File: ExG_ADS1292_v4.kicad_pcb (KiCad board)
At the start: 2 copper layers, 31.8 x 19.6 mm, 64 parts, among them P1 CONN_2, P2 CONN_2, P3 CONN_2, P4 CONN_1, P5 CONN_01X04, U1 TPS63001, U2 ADS1291/2, U3 NRF528XX-QFAA, U4 MPU-9250, U5 TPS2294x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

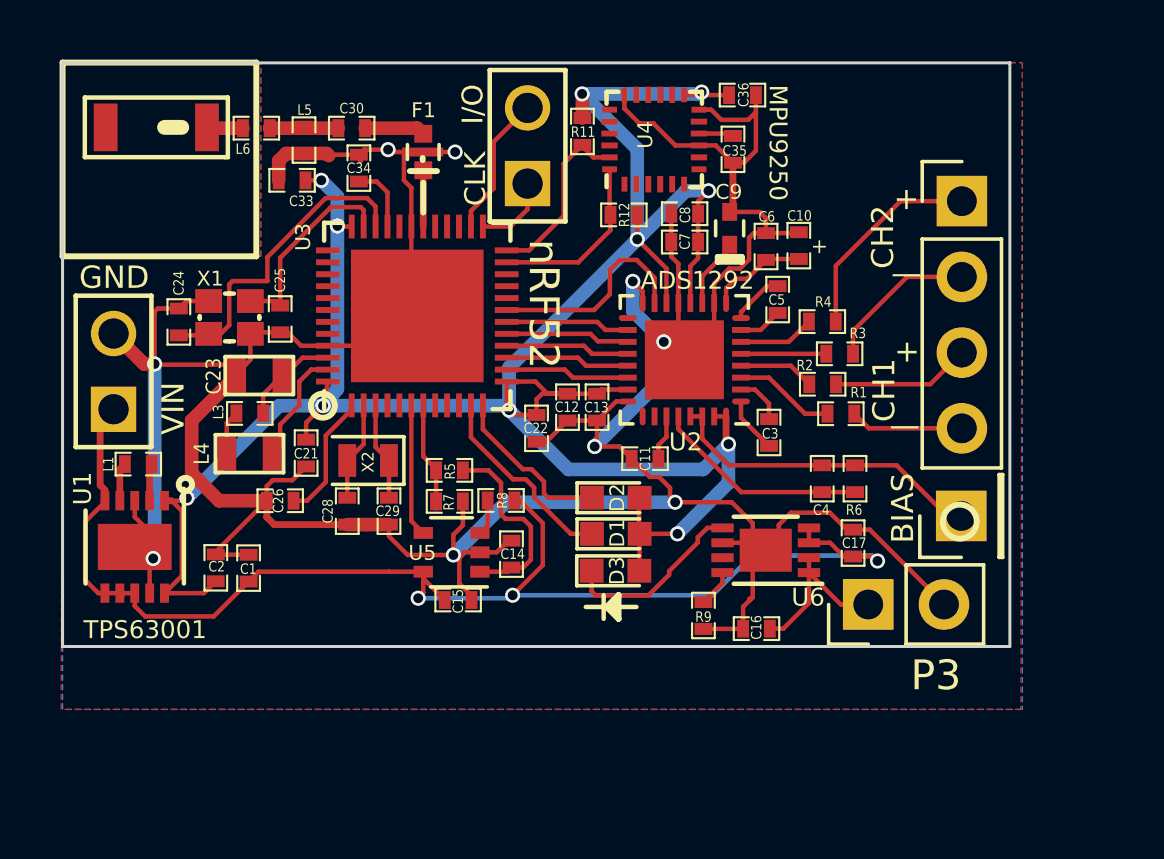
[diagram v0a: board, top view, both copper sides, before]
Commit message: Added updated recharging and load sharing circuit : extra components (Q1, D4, R10, C18).
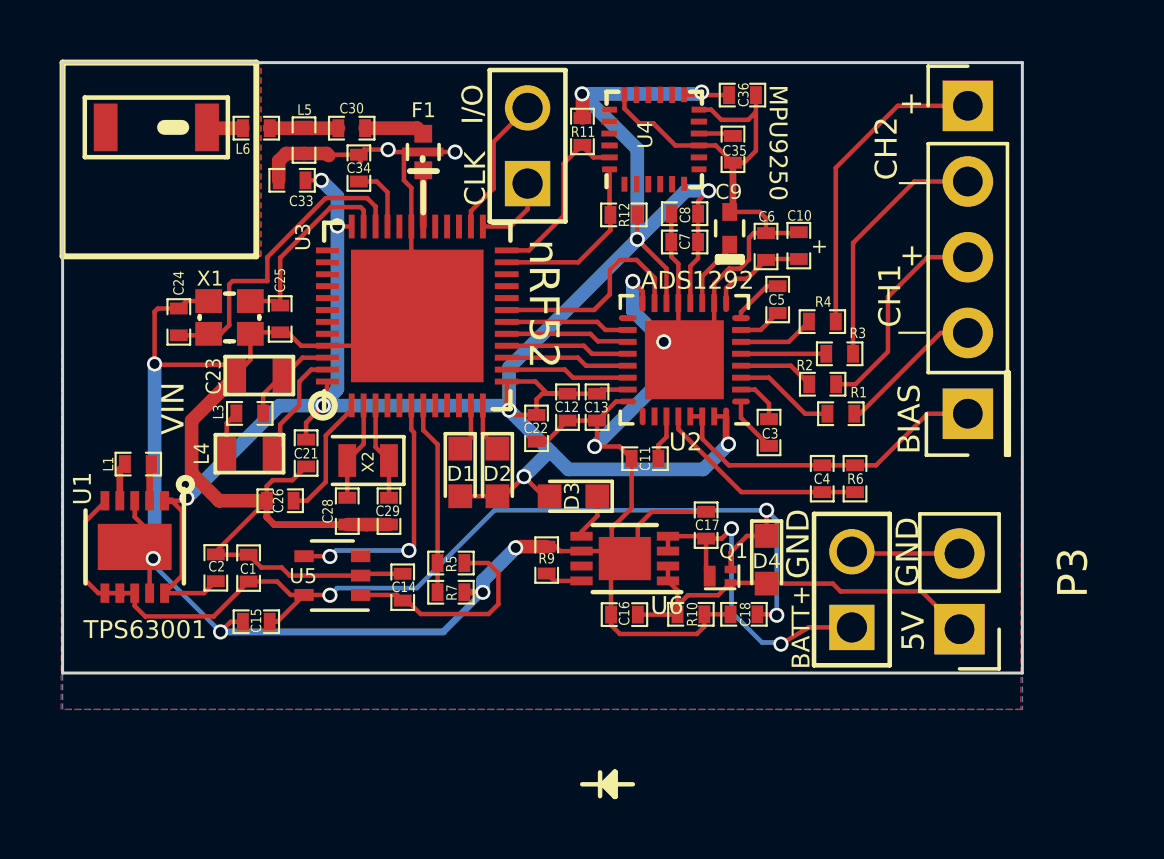
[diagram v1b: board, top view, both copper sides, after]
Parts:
- removed R8: N.C., SM0402
- added C18: 1.0uF, SM0402, F.Cu at (288.8, 144.0)
- added D4: D_Schottky, LEDs:LED_0603, F.Cu at (289.5, 142.2)
- added Q1: Q_PMOS_GDS, pwr_pads:X2-DFN1006, F.Cu at (288.0, 142.7)
- added R10: 100k, SM0402, F.Cu at (287.0, 144.0)
- moved P1 25.8 mm to (292.4, 143.2)
- moved C15 6.81 mm to (272.4, 144.3), turned to 180 degrees
- moved D1 5.61 mm to (279.2, 139.2), turned to 270 degrees
- moved R9 5.58 mm to (282.1, 142.2), turned to 90 degrees
- moved C17 4.97 mm to (287.5, 141.0)
- moved U6 4.74 mm to (284.8, 142.1)
- moved C16 4.45 mm to (284.8, 144.0)
- moved U5 4.08 mm to (274.9, 142.7)
- moved D2 4.06 mm to (280.5, 139.2), turned to 270 degrees
- moved C14 3.82 mm to (277.3, 143.1)
- moved P4 3.44 mm to (296.3, 137.3)
- moved P5 3.21 mm to (296.3, 127.0)
- moved P3 3.17 mm to (296.0, 144.5), turned to 180 degrees
- moved R5 3.11 mm to (278.9, 142.3)
- moved R7 3.05 mm to (278.9, 143.3)
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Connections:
- C17 pad 1: VCC -> /BATT_IN
- P1 pad 1: VCC -> /BATT_IN
- U6 pad 3: VCC -> /BATT_IN
- U6 pad 4: VCC -> /BATT_IN
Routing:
- net /BATT_IN: track 0.00 -> 11.5 mm, vias 0 -> 2
- net 5V_in_charge: track 5.62 -> 13.8 mm
- net VCC: track 44.5 -> 37.3 mm
- net /LED2: track 6.66 -> 1.60 mm
- net Net-(D3-Pad1): track 6.25 -> 1.56 mm
- net DGND: track 152.8 -> 157.3 mm, vias 9 -> 10
- net /LOAD_SW_CTRL: track 4.45 -> 8.58 mm, vias 0 -> 2
- net /LED3: track 5.63 -> 1.65 mm
- net /IN2: track 7.00 -> 10.5 mm
- net /IN2-: track 5.17 -> 8.42 mm
- net /AIN_BAT_DIV_VOLTAGE: track 3.77 -> 6.47 mm
- net DVDD: track 85.1 -> 82.4 mm
- net /IN1: track 4.66 -> 7.26 mm
- net Net-(R8-Pad1): track 1.20 -> 0.00 mm
- net /IN1-: track 3.81 -> 4.93 mm
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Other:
- board size 31.8 x 19.6 mm -> 32.2 x 20.5 mm
- board text added: "5V"
- board text added: "BATT+"

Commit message: Fixed load sharing circuit and PCB (final)
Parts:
- Q1: value Q_PMOS_GDS -> DMP21D5UFB4-7B
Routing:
- net DGND: track 157.3 -> 163.8 mm, vias 10 -> 11
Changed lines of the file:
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@@
     (links 185)
     (no_connects 0)
-    (area 265.849999 125.449999 297.730001 145.140001)
+    (area 264.8176 122.157123 320.907143 150.212501)
     (thickness 1.6)
     (drawings 47)
-    (tracks 546)
+    (tracks 552)
     (zones 0)
     (modules 67)
@@
   )
   (setup
-    (last_trace_width 0.152)
+    (last_trace_width 0.4572)
     (user_trace_width 0.152)
     (user_trace_width 0.229)
@@
       (effects (font (size 0.5 0.5) (thickness 0.08)))
     )
-    (fp_text value Q_PMOS_GDS (at 0.225 1.425 180) (layer F.Fab)
+    (fp_text value DMP21D5UFB4-7B (at 0.225 1.425 180) (layer F.Fab)
       (effects (font (size 1 1) (thickness 0.15)))
     )
@@
   (segment (start 280.9 131.8) (end 280.95 131.8) (width 0.152) (layer F.Cu) (net 54))
   (segment (start 280.9 131.8) (end 281.1 131.8) (width 0.1524) (layer F.Cu) (net 54))
+  (segment (start 287.49 140.57042) (end 287.49 140.08) (width 0.152) (layer F.Cu) (net 72))
+  (segment (start 290 139.53) (end 292.38 141.91) (width 0.229) (layer B.Cu) (net 72))
+  (segment (start 288.04 139.53) (end 290 139.53) (width 0.229) (layer B.Cu) (net 72))
+  (segment (start 287.74 139.83) (end 288.04 139.53) (width 0.229) (layer B.Cu) (net 72))
+  (via (at 287.74 139.83) (size 0.508) (drill 0.3302) (layers F.Cu B.Cu) (net 72))
+  (segment (start 287.49 140.08) (end 287.74 139.83) (width 0.152) (layer F.Cu) (net 72))
   (segment (start 284.30042 144.02) (end 284.30042 144.37042) (width 0.152) (layer F.Cu) (net 72))
   (segment (start 287.42958 144.42042) (end 287.42958 144.01) (width 0.152) (layer F.Cu) (net 72))

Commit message: Removed MPU9250 (EMG only with recharge circuit).
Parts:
- removed C35, C36: 100nF, SM0402
- removed R11, R12: 10k, SM0402
- removed U4: MPU-9250, Housings_DFN_QFN:QFN-24_3x3mm_Pitch0.4mm
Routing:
- net DVDD: track 82.4 -> 69.5 mm, vias 11 -> 9
- net DGND: track 163.8 -> 152.3 mm
- net /SCL: track 6.40 -> 0.25 mm
- net /SDI: track 5.98 -> 0.00 mm
- net Net-(C35-Pad1): track 1.17 -> 0.00 mm
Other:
- board text removed: "MPU9250"
